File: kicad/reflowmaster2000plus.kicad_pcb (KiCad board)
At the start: 2 copper layers, 46.6 x 24.1 mm, 34 parts, among them P1 CONN_02X04, P2 230V, P3 Toaster, U1 TLC2272, U2 MOC3063, U3 BTA24

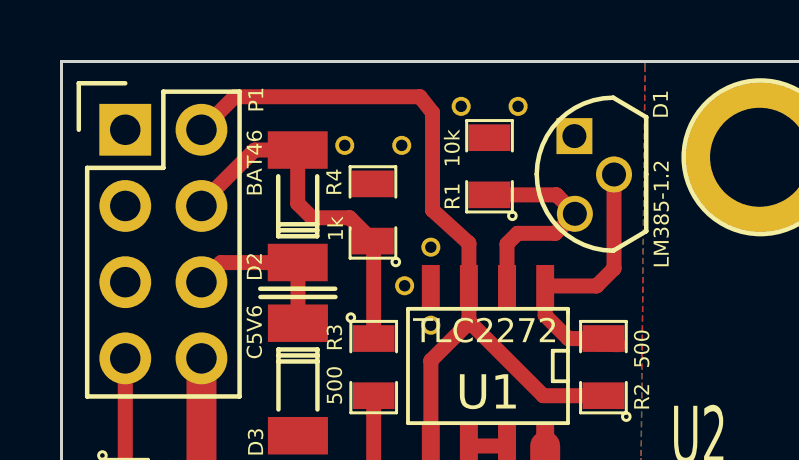
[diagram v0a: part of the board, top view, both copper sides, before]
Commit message: [enh] Kicad: v10 final SCH, PCB and gerbers. Client: Man strings. Graph drawing synced with the bake proces. Doc: some new papers about reflow technique, and OPA design.
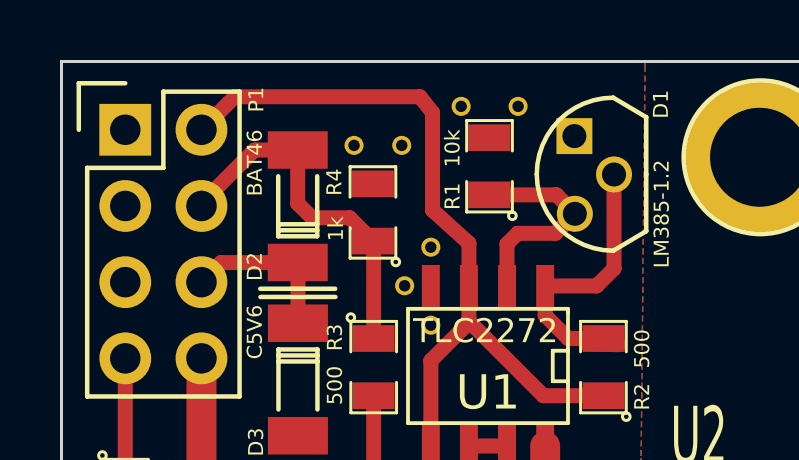
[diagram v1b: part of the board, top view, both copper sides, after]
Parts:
- moved 1Pin_15mil_VIA 0.31 mm to (164.9, 122.0)
